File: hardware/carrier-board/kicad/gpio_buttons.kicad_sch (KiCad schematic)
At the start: 0 parts

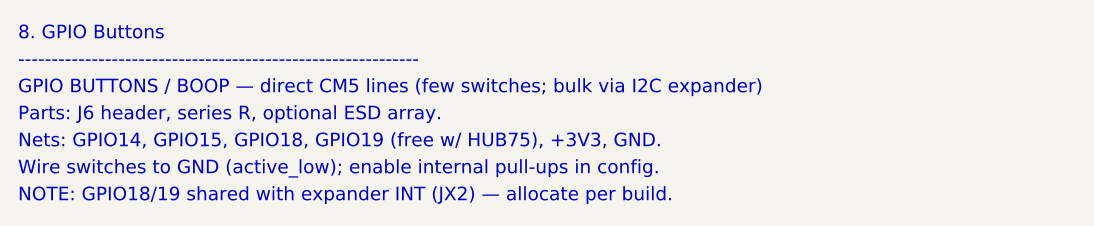
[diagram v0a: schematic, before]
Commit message: Carrier docs + KiCad plan: full two-brain pass (CM5 HUB75 + RP2354B I/O)
Propagate the two-brain architecture across the whole doc set and KiCad plan:
- REQUIREMENTS: restructured M1-M12 (CM5 HUB75; RP2354B core/MAX7219/WS2812/
  sensors/buttons/servos; USB selector + standalone program port); N-list reworked.
- POWER: add +V_SERVO and +3V3_RP rails, servo current budget, updated worked
  total + protection; sensors now on +3V3_RP not CM5 3V3.
- CONNECTORS: J3 re-sourced to RP2354B SPI0, J4 4 WS2812 zones, J5 +SENS_INT,
  J6 BTN1..10, add J12 USB-C, J20-J27 servos, SW1 USB selector, SWD/UART hdrs;
  drop JP1/JP2; fans presented as RP2354B-default-or-CM5 (decision flagged).
- BOM: add RP2354B core, '125/'245 (RP side), USB mux/USB-C/ESD, servo headers,
  +3V3_RP reg; fix '125 double-count and stale HUB75/MAX7219-shared-buffer/JP1.
- MULTI-BACKEND: HUB75+MAX7219 now simultaneous (different brains); firmware
  CompositePanelOutput is the sole remaining blocker.
- IO-EXPANSION: RP2354B is the primary I/O backbone; I2C expanders secondary.
- kicad: 11-sheet plan, stable UUIDs, generator skips populated face_buffer.
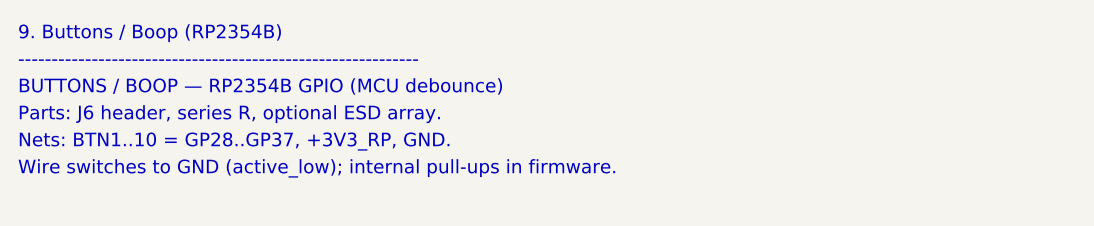
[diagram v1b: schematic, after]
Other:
- note added: "9. Buttons / Boop (RP2354B)"
- note added: "BUTTONS / BOOP — RP2354B GPIO (MCU debounce)"
- note added: "Nets: BTN1..10 = GP28..GP37, +3V3_RP, GND."
- note added: "Wire switches to GND (active_low); internal pull-ups in firmware."
- note removed: "8. GPIO Buttons"
- note removed: "GPIO BUTTONS / BOOP — direct CM5 lines (few switches; bulk via I2C expander)"
- note removed: "NOTE: GPIO18/19 shared with expander INT (JX2) — allocate per build."
- note removed: "Nets: GPIO14, GPIO15, GPIO18, GPIO19 (free w/ HUB75), +3V3, GND."
- note removed: "Wire switches to GND (active_low); enable internal pull-ups in config."
- title: ProtoHUD Carrier — 8. GPIO Buttons -> ProtoHUD Carrier — 9. Buttons / Boop (RP2354B)
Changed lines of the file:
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@@
   (paper "A3")
   (title_block
-    (title "ProtoHUD Carrier — 8. GPIO Buttons")
+    (title "ProtoHUD Carrier — 9. Buttons / Boop (RP2354B)")
     (rev "A")
     (company "ProtoHUD")
   )
-  (text "8. GPIO Buttons" (at 25.4 25.40 0) (effects (font (size 1.5 1.5)) (justify left bottom)))
+  (text "9. Buttons / Boop (RP2354B)" (at 25.4 25.40 0) (effects (font (size 1.5 1.5)) (justify left bottom)))
   (text "------------------------------------------------------------" (at 25.4 28.40 0) (effects (font (size 1.5 1.5)) (justify left bottom)))
-  (text "GPIO BUTTONS / BOOP — direct CM5 lines (few switches; bulk via I2C expander)" (at 25.4 31.40 0) (effects (font (size 1.5 1.5)) (justify left bottom)))
+  (text "BUTTONS / BOOP — RP2354B GPIO (MCU debounce)" (at 25.4 31.40 0) (effects (font (size 1.5 1.5)) (justify left bottom)))
   (text "Parts: J6 header, series R, optional ESD array." (at 25.4 34.40 0) (effects (font (size 1.5 1.5)) (justify left bottom)))
-  (text "Nets: GPIO14, GPIO15, GPIO18, GPIO19 (free w/ HUB75), +3V3, GND." (at 25.4 37.40 0) (effects (font (size 1.5 1.5)) (justify left bottom)))
-  (text "Wire switches to GND (active_low); enable internal pull-ups in config." (at 25.4 40.40 0) (effects (font (size 1.5 1.5)) (justify left bottom)))
-  (text "NOTE: GPIO18/19 shared with expander INT (JX2) — allocate per build." (at 25.4 43.40 0) (effects (font (size 1.5 1.5)) (justify left bottom)))
+  (text "Nets: BTN1..10 = GP28..GP37, +3V3_RP, GND." (at 25.4 37.40 0) (effects (font (size 1.5 1.5)) (justify left bottom)))
+  (text "Wire switches to GND (active_low); internal pull-ups in firmware." (at 25.4 40.40 0) (effects (font (size 1.5 1.5)) (justify left bottom)))
   (sheet_instances
     (path "/" (page "1"))

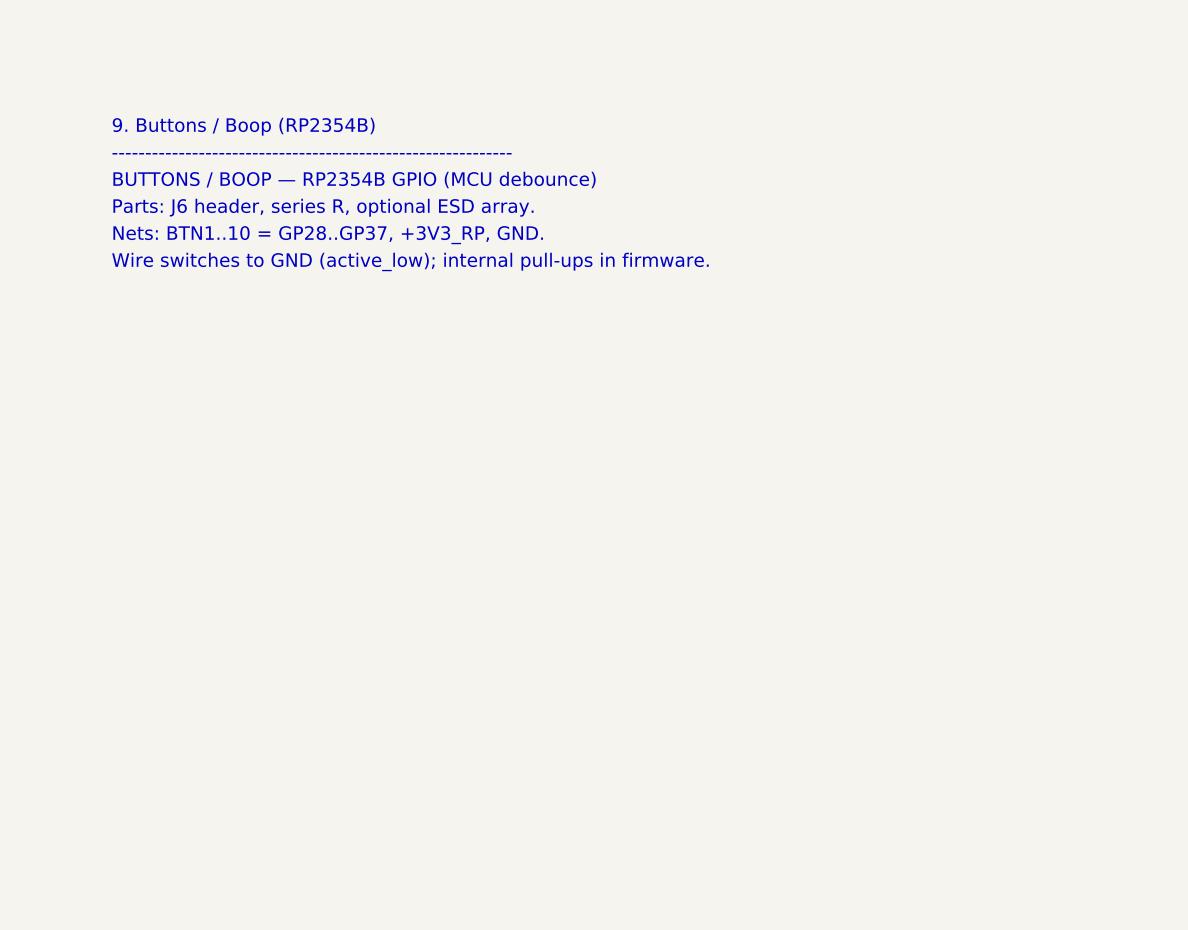
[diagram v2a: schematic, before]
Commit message: Carrier KiCad: populate all 11 schematic sheets
Replace populate_face_buffer.py with populate_sheets.py: one generator that
emits all 11 populated sub-sheets reusing the KiCad-9 format proven by the
face_buffer proof. Shared symbol library + generic box-symbol builder; condensed
CM5 (2x DF40-100) and RP2354B (QFN-80) symbols showing only used pins.

Connectivity by net labels (global for rails + cross-sheet nets: GPIOxx HUB75,
MX_*, LED*_DAT, SRV*, BTN*, *_USB_*; local within-sheet). Sheets: power
(protection + rails + AP2112 +3V3_RP), cm5 (HUB75 out + fan MOSFETs + RP ctrl),
face_buffer, rp2354_io (RP2354B + xtal + SW1/J12 + ESD + SWD), rp2354_face
(U10->J3), leds (U11 quad ->J4a-d), sensors_i2c (pull-ups+J5+STEMMA),
servos (J20-27 + rail), gpio_buttons (J6), usb (USB2514B hub + uplink),
cameras_display (CSI FFC + HDMI).

Verified: all sheets paren-balanced, every used lib_id defined, all instance
paths match sheet UUIDs, root<->sub-sheet UUID linkage intact. generate_skeleton.py
now lists all sheets POPULATED (writes only root+project). Not yet opened in
KiCad here -- expect ERC warnings (PWR_FLAG, unconnected pins) to clean.
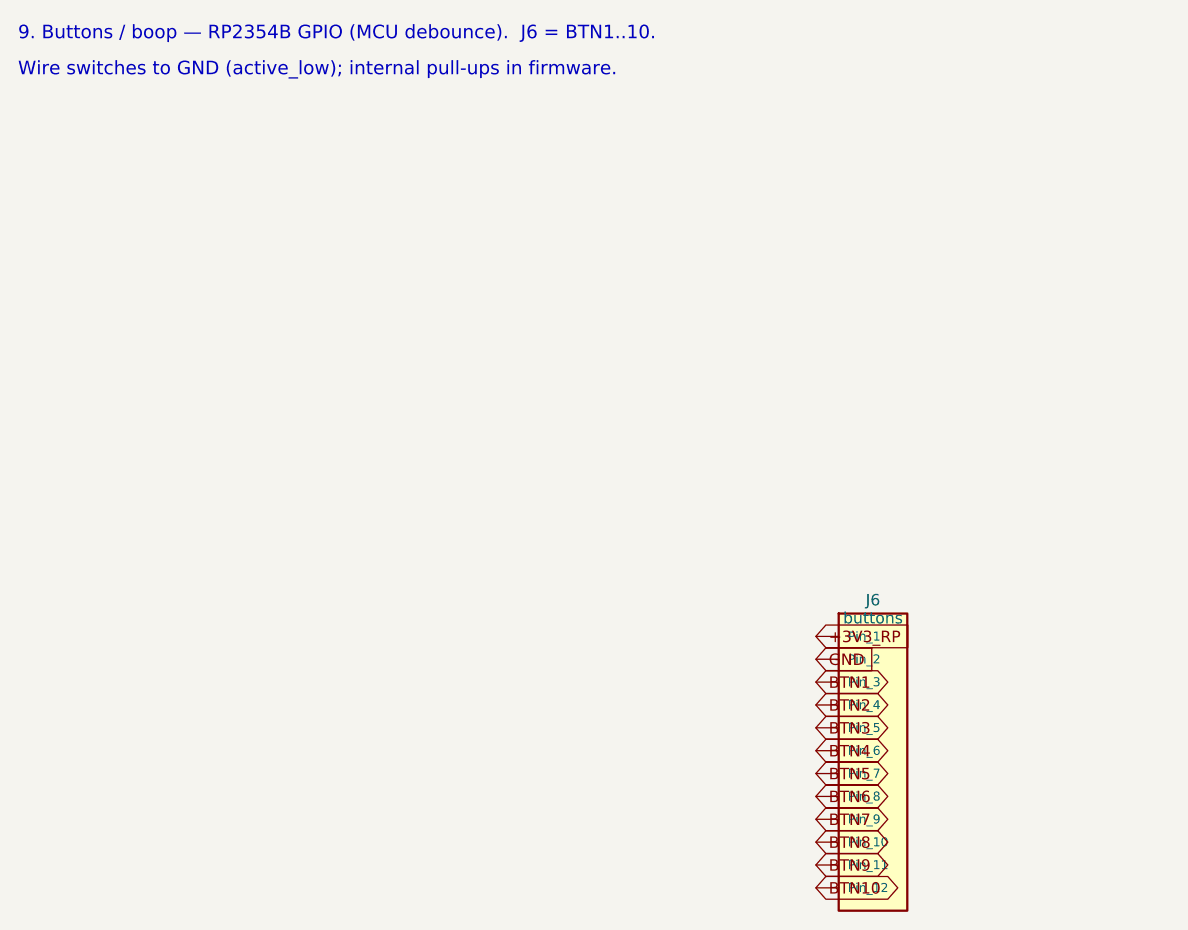
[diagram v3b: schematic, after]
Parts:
- added J6: buttons, symbol Connector_Generic:Conn_01x12
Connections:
- new net +3V3_RP: J6.1 (Pin_1)
- new net BTN1: J6.3 (Pin_3)
- new net BTN10: J6.12 (Pin_12)
- new net BTN2: J6.4 (Pin_4)
- new net BTN3: J6.5 (Pin_5)
- new net BTN4: J6.6 (Pin_6)
- new net BTN5: J6.7 (Pin_7)
- new net BTN6: J6.8 (Pin_8)
- new net BTN7: J6.9 (Pin_9)
- new net BTN8: J6.10 (Pin_10)
- new net BTN9: J6.11 (Pin_11)
- new net GND: J6.2 (Pin_2)
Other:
- note added: "9. Buttons / boop — RP2354B GPIO (MCU debounce). J6 = BTN1..10."
- note removed: "------------------------------------------------------------"
- note removed: "9. Buttons / Boop (RP2354B)"
- note removed: "BUTTONS / BOOP — RP2354B GPIO (MCU debounce)"
- note removed: "Nets: BTN1..10 = GP28..GP37, +3V3_RP, GND."
- note removed: "Parts: J6 header, series R, optional ESD array."
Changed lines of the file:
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@@
 (kicad_sch
-  (version 20230121)
-  (generator protohud_skeleton)
+  (version 20250114)
+  (generator "protohud_populate")
+  (generator_version "9.0")
   (paper "A3")
   (title_block
@@
     (company "ProtoHUD")
   )
-  (text "9. Buttons / Boop (RP2354B)" (at 25.4 25.40 0) (effects (font (size 1.5 1.5)) (justify left bottom)))
-  (text "------------------------------------------------------------" (at 25.4 28.40 0) (effects (font (size 1.5 1.5)) (justify left bottom)))
-  (text "BUTTONS / BOOP — RP2354B GPIO (MCU debounce)" (at 25.4 31.40 0) (effects (font (size 1.5 1.5)) (justify left bottom)))
-  (text "Parts: J6 header, series R, optional ESD array." (at 25.4 34.40 0) (effects (font (size 1.5 1.5)) (justify left bottom)))
-  (text "Nets: BTN1..10 = GP28..GP37, +3V3_RP, GND." (at 25.4 37.40 0) (effects (font (size 1.5 1.5)) (justify left bottom)))
-  (text "Wire switches to GND (active_low); internal pull-ups in firmware." (at 25.4 40.40 0) (effects (font (size 1.5 1.5)) (justify left bottom)))
+  (text "9. Buttons / boop — RP2354B GPIO (MCU debounce).  J6 = BTN1..10." (at 15 15.0 0) (effects (font (size 1.5 1.5)) (justify left bottom)))
+  (text "Wire switches to GND (active_low); internal pull-ups in firmware." (at 15 19.0 0) (effects (font (size 1.5 1.5)) (justify left bottom)))
+  (symbol
+    (lib_id "Connector_Generic:Conn_01x12")
+    (at 110.00 95.00 0)
+    (unit 1)
+    (exclude_from_sim no) (in_bom yes) (on_board yes) (dnp no)
+    (property "Reference" "J6" (at 110.00 77.00 0) (effects (font (size 1.27 1.27))))
+    (property "Value" "buttons" (at 110.00 79.00 0) (effects (font (size 1.27 1.27))))
+    (property "Footprint" "" (at 110.00 95.00 0) (effects (font (size 1.27 1.27)) (hide yes)))
+    (property "Datasheet" "" (at 110.00 95.00 0) (effects (font (size 1.27 1.27)) (hide yes)))
+    (pin "1")
+    (pin "2")
+    (pin "3")
+    (pin "4")
+    (pin "5")
+    (pin "6")
+    (pin "7")
+    (pin "8")
+    (pin "9")
+    (pin "10")
+    (pin "11")
+    (pin "12")
+    (instances
+      (project "ProtoHUD-Carrier"
+        (path "/4d61ad14-7947-4b5f-b9ac-ea72b52475d0"
+          (reference "J6") (unit 1))))
+  )
+  (global_label "+3V3_RP" (shape input) (at 103.65 81.03 180) (effects (font (size 1.27 1.27)) (justify left)))
+  (global_label "GND" (shape input) (at 103.65 83.57 180) (effects (font (size 1.27 1.27)) (justify left)))
+  (global_label "BTN1" (shape bidirectional) (at 103.65 86.11 180) (effects (font (size 1.27 1.27)) (justify left)))
+  (global_label "BTN2" (shape bidirectional) (at 103.65 88.65 180) (effects (font (size 1.27 1.27)) (justify left)))
+  (global_label "BTN3" (shape bidirectional) (at 103.65 91.19 180) (effects (font (size 1.27 1.27)) (justify left)))
+  (global_label "BTN4" (shape bidirectional) (at 103.65 93.73 180) (effects (font (size 1.27 1.27)) (justify left)))
+  (global_label "BTN5" (shape bidirectional) (at 103.65 96.27 180) (effects (font (size 1.27 1.27)) (justify left)))
+  (global_label "BTN6" (shape bidirectional) (at 103.65 98.81 180) (effects (font (size 1.27 1.27)) (justify left)))
+  (global_label "BTN7" (shape bidirectional) (at 103.65 101.35 180) (effects (font (size 1.27 1.27)) (justify left)))
+  (global_label "BTN8" (shape bidirectional) (at 103.65 103.89 180) (effects (font (size 1.27 1.27)) (justify left)))
+  (global_label "BTN9" (shape bidirectional) (at 103.65 106.43 180) (effects (font (size 1.27 1.27)) (justify left)))
+  (global_label "BTN10" (shape bidirectional) (at 103.65 108.97 180) (effects (font (size 1.27 1.27)) (justify left)))
   (sheet_instances
     (path "/" (page "1"))
